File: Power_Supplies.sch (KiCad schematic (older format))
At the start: 38 parts, among them J1 Conn_HDR_2x10_latching, Q3 2N7002BK, Q4 2N7002BK, Q5 2N7002BK, Q6 2N7002BK, Q7 2N7002BK, Q8 2N7002BK, Q9 2N7002BK, U4 BD50FC0WEFJ-E2, U5 LDL212D33R, U6 LDL212D33R, U7 TLV7042DGKR

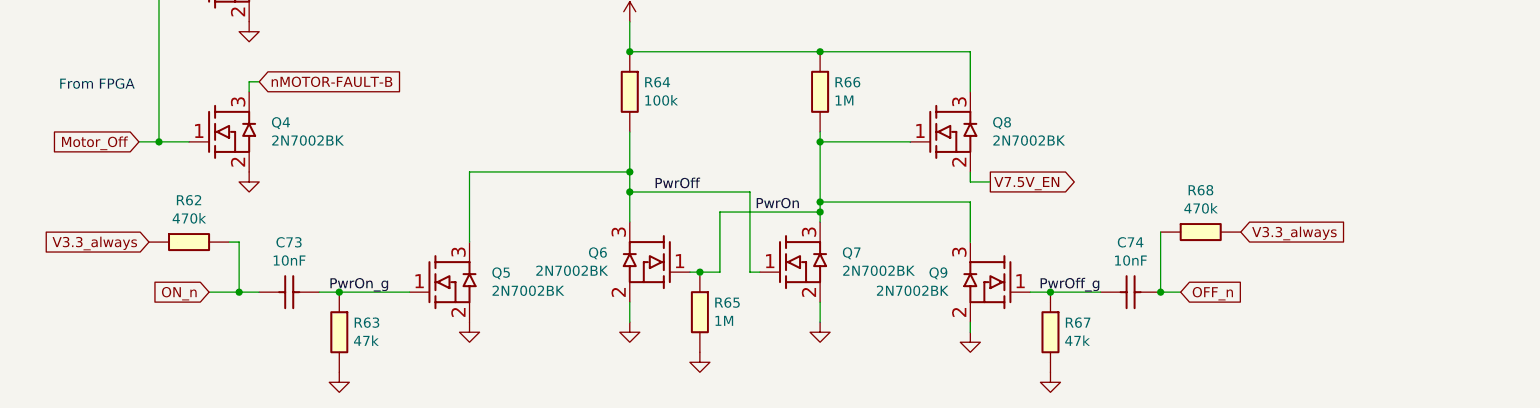
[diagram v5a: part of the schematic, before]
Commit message: Corrected power ON/OFF control circuit signal labels
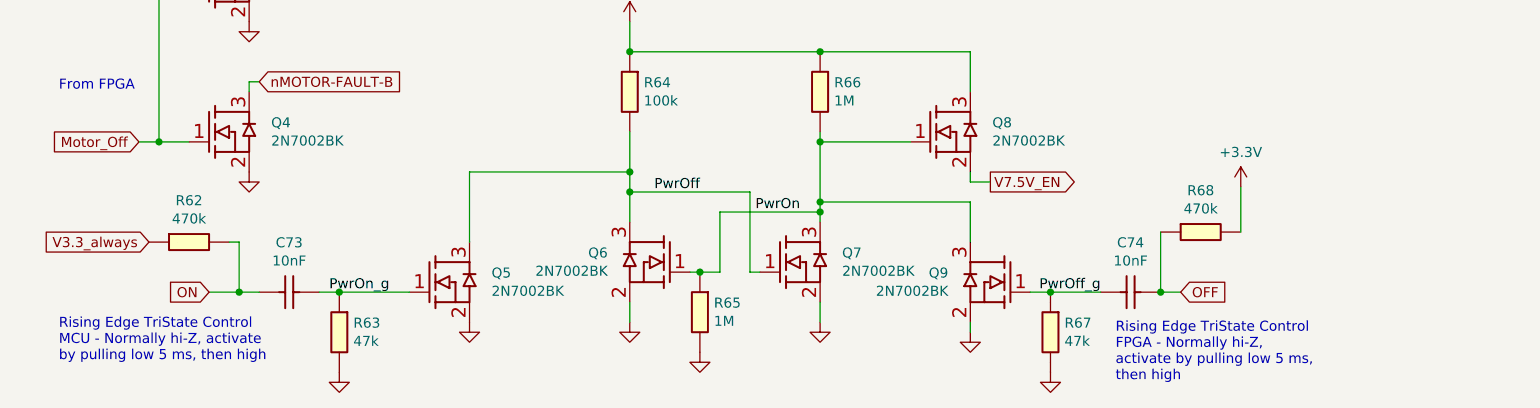
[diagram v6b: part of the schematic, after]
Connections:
- net +3V3: now also R68.2
- net V3.3_always: no longer R68.2
- net OFF_n renamed OFF
- net ON_n renamed ON
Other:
- note added: "Rising Edge TriState Control\nFPGA - Normally hi-Z,\nactivate by pulling low 5 ms,\nthen high"
- note added: "Rising Edge TriState Control\nMCU - Normally hi-Z, activate \nby pulling low 5 ms, then high"
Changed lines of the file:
@@
 	1450 7300 1550 7300
 Text GLabel 1300 7300 0    50   Input ~ 0
-ON_n
+ON
 Wire Wire Line
 	1300 7300 1450 7300
@@
 $EndComp
 Text GLabel 6150 7300 2    50   Input ~ 0
-OFF_n
+OFF
 Wire Wire Line
 	6050 7300 6150 7300
+Connection ~ 6050 7300
+Text Label 2200 7300 2    50   ~ 0
+PwrOn_g
+Text Label 3750 6800 2    50   ~ 0
+PwrOff
+Text Label 4250 6900 2    50   ~ 0
+PwrOn
+Text Label 5750 7300 2    50   ~ 0
+PwrOff_g
+$Comp
+L OpenVent:1M_0603_Chip_Resistor,_1%,_0.1W R66
+U 1 1 60119693
+P 4450 6200
+F 0 "R66" V 4504 6170 50  0000 L CNN
+F 1 "1M_0603_Chip_Resistor,_1%,_0.1W" H 4450 6200 50  0001 C CNN
+F 2 "" H 4450 6200 50  0001 C CNN
+F 3 "" H 4450 6200 50  0001 C CNN
+F 4 "1M" V 4595 6170 50  0000 L CNN "Val"
+F 5 "1%" H 4450 6200 50  0001 C CNN "Tolerance"
+F 6 "0.1W" H 4450 6200 50  0001 C CNN "Watt"
+	1    4450 6200
+	0    1    1    0
+$EndComp
+Connection ~ 4350 6550
+Wire Wire Line
+	4350 6550 4350 6850
+Connection ~ 4350 6100
+Wire Wire Line
+	4350 6100 3400 6100
+Wire Wire Line
+	4350 6500 4350 6550
+Wire Wire Line
+	3400 6700 3400 6500
+Connection ~ 3400 6700
+Wire Wire Line
+	5100 6100 5100 6300
+$Comp
+L OpenVent:1M_0603_Chip_Resistor,_1%,_0.1W R65
+U 1 1 6013F297
+P 3850 7300
+F 0 "R65" V 3904 7270 50  0000 L CNN
+F 1 "1M_0603_Chip_Resistor,_1%,_0.1W" H 3850 7300 50  0001 C CNN
+F 2 "" H 3850 7300 50  0001 C CNN
+F 3 "" H 3850 7300 50  0001 C CNN
+F 4 "1M" V 3995 7270 50  0000 L CNN "Val"
+F 5 "1%" H 3850 7300 50  0001 C CNN "Tolerance"
+F 6 "0.1W" H 3850 7300 50  0001 C CNN "Watt"
+	1    3850 7300
+	0    1    1    0
+$EndComp
+Connection ~ 3750 7200
+Wire Wire Line
+	3750 7200 3850 7200
+$Comp
+L OpenVent:47k_0603_Chip_Resistor,_1%,_0.1W R63
+U 1 1 60168217
+P 2050 7400
+F 0 "R63" V 2104 7370 50  0000 L CNN
+F 1 "47k_0603_Chip_Resistor,_1%,_0.1W" H 2050 7400 50  0001 C CNN
+F 2 "" H 2050 7400 50  0001 C CNN
+F 3 "" H 2050 7400 50  0001 C CNN
+F 4 "47k" V 2195 7370 50  0000 L CNN "Val"
+F 5 "1%" H 2050 7400 50  0001 C CNN "Tolerance"
+F 6 "0.1W" H 2050 7400 50  0001 C CNN "Watt"
+	1    2050 7400
+	0    1    1    0
+$EndComp
+$Comp
+L OpenVent:47k_0603_Chip_Resistor,_1%,_0.1W R67
+U 1 1 60168F63
+P 5600 7400
+F 0 "R67" V 5654 7370 50  0000 L CNN
+F 1 "47k_0603_Chip_Resistor,_1%,_0.1W" H 5600 7400 50  0001 C CNN
+F 2 "" H 5600 7400 50  0001 C CNN
+F 3 "" H 5600 7400 50  0001 C CNN
+F 4 "47k" V 5745 7370 50  0000 L CNN "Val"
+F 5 "1%" H 5600 7400 50  0001 C CNN "Tolerance"
+F 6 "0.1W" H 5600 7400 50  0001 C CNN "Watt"
+	1    5600 7400
+	0    1    1    0
+$EndComp
+Connection ~ 1950 7300
+Wire Wire Line
+	1950 7300 2300 7300
+Connection ~ 5500 7300
+Wire Wire Line
+	5500 7300 5750 7300
+$Comp
+L OpenVent:V_MAIN #PWR0112
+U 1 1 60198400
+P 3400 5950
+F 0 "#PWR0112" H 3400 5800 50  0001 C CNN
+F 1 "V_MAIN" H 3400 6123 50  0000 C CNN
+F 2 "" H 3400 5950 50  0001 C CNN
+F 3 "" H 3400 5950 50  0001 C CNN
+	1    3400 5950
+	1    0    0    -1
+$EndComp
+Wire Wire Line
+	3400 6100 3400 5950
+Wire Wire Line
+	1500 6300 1500 6250
+Wire Wire Line
+	1500 6250 1550 6250
+Wire Wire Line
+	1500 5550 1500 5500
+Wire Wire Line
+	1500 5500 1550 5500
+Wire Wire Line
+	5200 6750 5100 6750
+Wire Wire Line
+	5100 6750 5100 6700
+$Comp
+L OpenVent:+3.3V #PWR?
+U 1 1 6007611B
+P 6450 6775
+F 0 "#PWR?" H 6450 6625 50  0001 C CNN
+F 1 "+3.3V" H 6450 6948 50  0000 C CNN
+F 2 "" H 6450 6775 50  0001 C CNN
+F 3 "" H 6450 6775 50  0001 C CNN
+	1    6450 6775
+	1    0    0    -1
+$EndComp
 $Comp
 L OpenVent:470k_0603_Chip_Resistor,_1%,_0.1W R68
@@
 $EndComp
 Wire Wire Line
-	6050 7300 6050 7000
-Text GLabel 6450 7000 2    50   Input ~ 0
-V3.3_always
-Connection ~ 6050 7300
-Text Label 2200 7300 2    50   ~ 0
-PwrOn_g
-Text Label 3750 6800 2    50   ~ 0
-PwrOff
-Text Label 4250 6900 2    50   ~ 0
-PwrOn
-Text Label 5750 7300 2    50   ~ 0
-PwrOff_g
-$Comp
-L OpenVent:1M_0603_Chip_Resistor,_1%,_0.1W R66
-U 1 1 60119693
-P 4450 6200
-F 0 "R66" V 4504 6170 50  0000 L CNN
-F 1 "1M_0603_Chip_Resistor,_1%,_0.1W" H 4450 6200 50  0001 C CNN
-F 2 "" H 4450 6200 50  0001 C CNN
-F 3 "" H 4450 6200 50  0001 C CNN
-F 4 "1M" V 4595 6170 50  0000 L CNN "Val"
-F 5 "1%" H 4450 6200 50  0001 C CNN "Tolerance"
-F 6 "0.1W" H 4450 6200 50  0001 C CNN "Watt"
-	1    4450 6200
-	0    1    1    0
-$EndComp
-Connection ~ 4350 6550
-Wire Wire Line
-	4350 6550 4350 6850
-Connection ~ 4350 6100
-Wire Wire Line
-	4350 6100 3400 6100
-Wire Wire Line
-	4350 6500 4350 6550
-Wire Wire Line
-	3400 6700 3400 6500
-Connection ~ 3400 6700
-Wire Wire Line
-	5100 6100 5100 6300
-$Comp
-L OpenVent:1M_0603_Chip_Resistor,_1%,_0.1W R65
-U 1 1 6013F297
-P 3850 7300
-F 0 "R65" V 3904 7270 50  0000 L CNN
-F 1 "1M_0603_Chip_Resistor,_1%,_0.1W" H 3850 7300 50  0001 C CNN
-F 2 "" H 3850 7300 50  0001 C CNN
-F 3 "" H 3850 7300 50  0001 C CNN
-F 4 "1M" V 3995 7270 50  0000 L CNN "Val"
-F 5 "1%" H 3850 7300 50  0001 C CNN "Tolerance"
-F 6 "0.1W" H 3850 7300 50  0001 C CNN "Watt"
-	1    3850 7300
-	0    1    1    0
-$EndComp
-Connection ~ 3750 7200
-Wire Wire Line
-	3750 7200 3850 7200
-$Comp
-L OpenVent:47k_0603_Chip_Resistor,_1%,_0.1W R63
-U 1 1 60168217
-P 2050 7400
-F 0 "R63" V 2104 7370 50  0000 L CNN
-F 1 "47k_0603_Chip_Resistor,_1%,_0.1W" H 2050 7400 50  0001 C CNN
-F 2 "" H 2050 7400 50  0001 C CNN
-F 3 "" H 2050 7400 50  0001 C CNN
-F 4 "47k" V 2195 7370 50  0000 L CNN "Val"
-F 5 "1%" H 2050 7400 50  0001 C CNN "Tolerance"
-F 6 "0.1W" H 2050 7400 50  0001 C CNN "Watt"
-	1    2050 7400
-	0    1    1    0
-$EndComp
-$Comp
-L OpenVent:47k_0603_Chip_Resistor,_1%,_0.1W R67
-U 1 1 60168F63
-P 5600 7400
-F 0 "R67" V 5654 7370 50  0000 L CNN
-F 1 "47k_0603_Chip_Resistor,_1%,_0.1W" H 5600 7400 50  0001 C CNN
-F 2 "" H 5600 7400 50  0001 C CNN
-F 3 "" H 5600 7400 50  0001 C CNN
-F 4 "47k" V 5745 7370 50  0000 L CNN "Val"
-F 5 "1%" H 5600 7400 50  0001 C CNN "Tolerance"
-F 6 "0.1W" H 5600 7400 50  0001 C CNN "Watt"
-	1    5600 7400
-	0    1    1    0
-$EndComp
-Connection ~ 1950 7300
-Wire Wire Line
-	1950 7300 2300 7300
-Connection ~ 5500 7300
-Wire Wire Line
-	5500 7300 5750 7300
-$Comp
-L OpenVent:V_MAIN #PWR0112
-U 1 1 60198400
-P 3400 5950
-F 0 "#PWR0112" H 3400 5800 50  0001 C CNN
-F 1 "V_MAIN" H 3400 6123 50  0000 C CNN
-F 2 "" H 3400 5950 50  0001 C CNN
-F 3 "" H 3400 5950 50  0001 C CNN
-	1    3400 5950
-	1    0    0    -1
-$EndComp
-Wire Wire Line
-	3400 6100 3400 5950
-Wire Wire Line
-	1500 6300 1500 6250
-Wire Wire Line
-	1500 6250 1550 6250
-Wire Wire Line
-	1500 5550 1500 5500
-Wire Wire Line
-	1500 5500 1550 5500
-Wire Wire Line
-	5200 6750 5100 6750
-Wire Wire Line
-	5100 6750 5100 6700
+	6050 7000 6050 7300
+Wire Wire Line
+	6450 7000 6450 6775
+Text Notes 5825 7750 0    50   ~ 0
+Rising Edge TriState Control\nFPGA - Normally hi-Z,\nactivate by pulling low 5 ms,\nthen high
+Text Notes 550  7650 0    50   ~ 0
+Rising Edge TriState Control\nMCU - Normally hi-Z, activate \nby pulling low 5 ms, then high
 $EndSCHEMATC

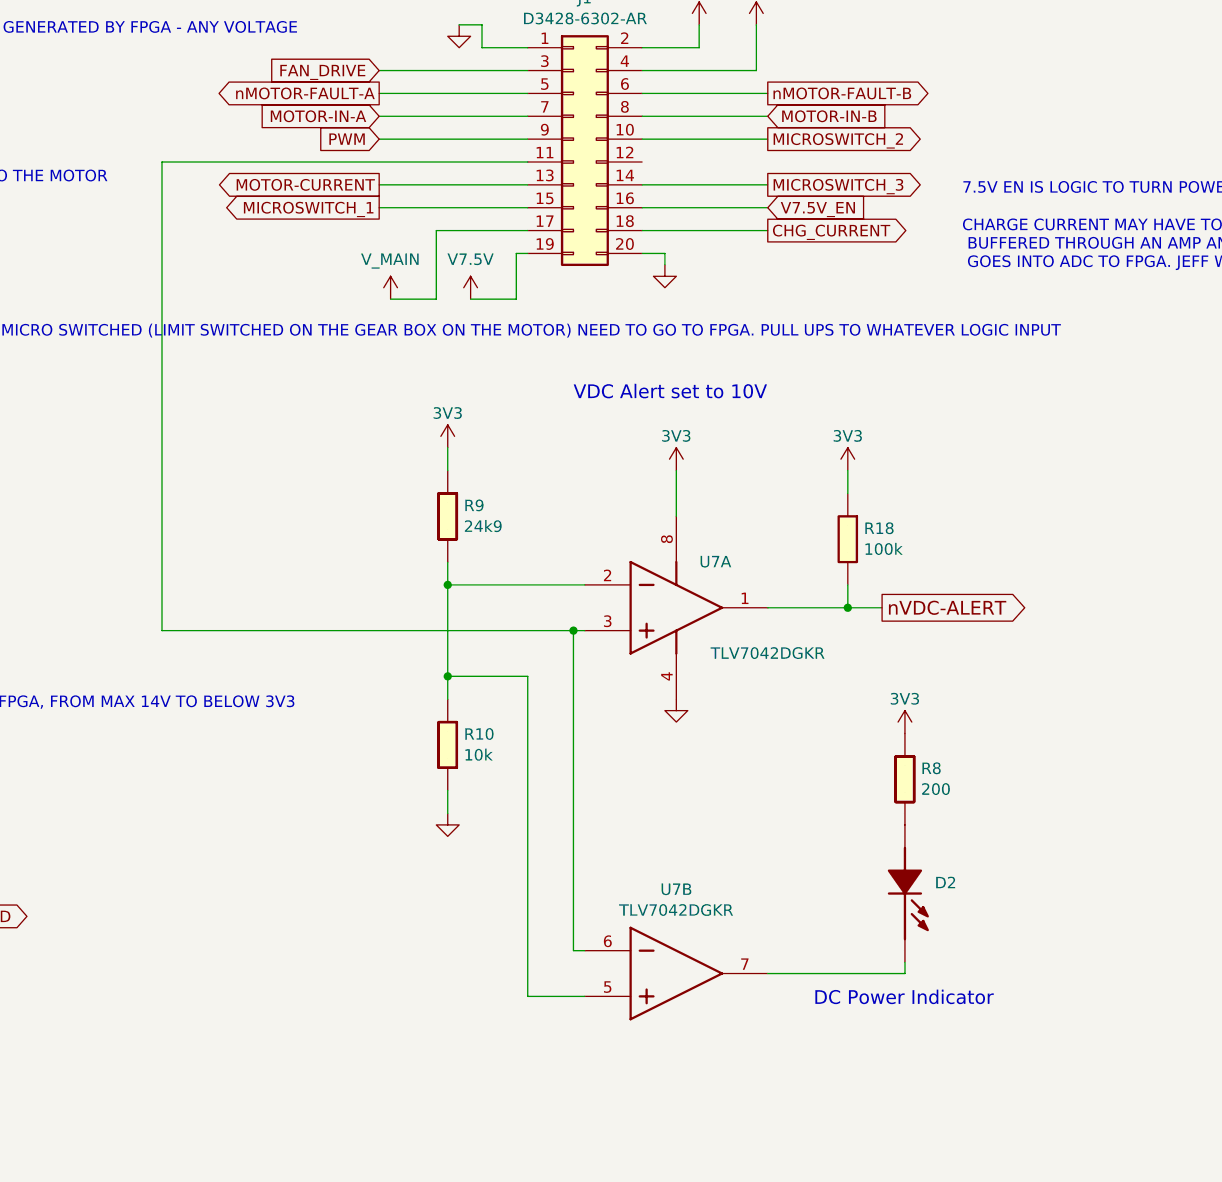
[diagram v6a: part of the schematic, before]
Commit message: Alerts and ISNS signals removed
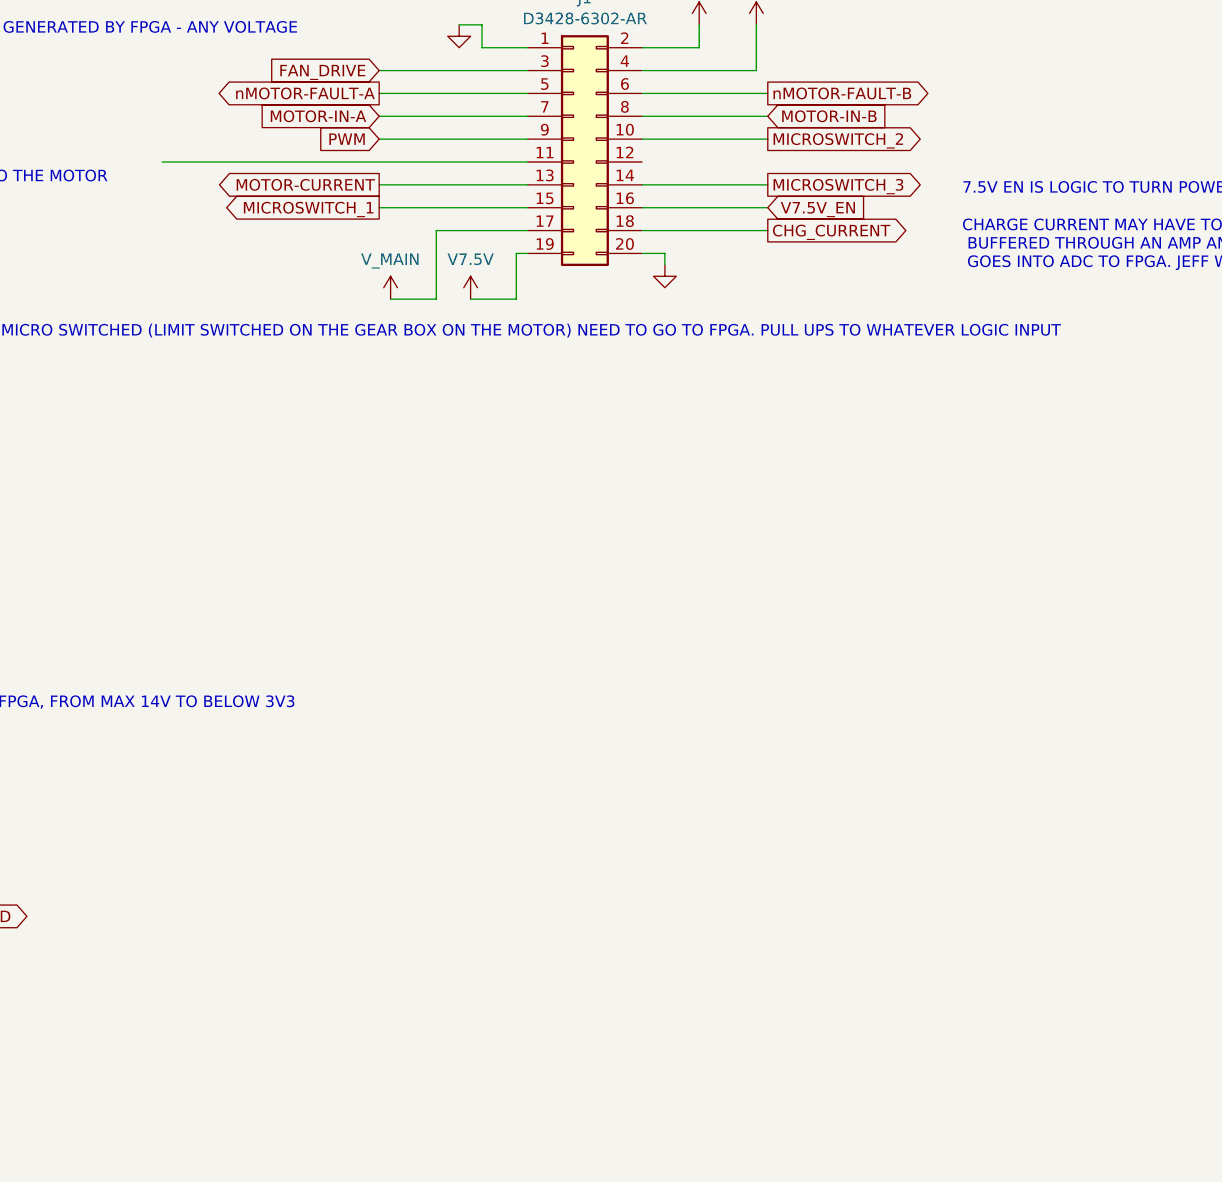
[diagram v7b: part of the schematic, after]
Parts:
- removed D2: LED_GREEN_0603_SMD, LED_SMD:LED_0603_1608Metric, symbol OpenVent:LED_GREEN_0603_SMD
- removed R10: 10k_0603_Chip_Resistor,_1%,_0.1W, Resistor_SMD:R_0603_1608Metric, symbol OpenVent:10k_0603_Chip_Resistor,_1%,_0.1W
- removed R18: 100K_0603_Chip_Resistor,_1%,_0.1W, Resistor_SMD:R_0603_1608Metric, symbol OpenVent:100K_0603_Chip_Resistor,_1%,_0.1W
- removed R8: R_0603_200_0.1W_1%, Resistor_SMD:R_0603_1608Metric, symbol OpenVent:R_0603_200_0.1W_1%
- removed R9: R_0603_24k9_0.1W_1%, symbol OpenVent:R_0603_24k9_0.1W_1%
- removed U7: TLV7042DGKR, F_ICs:Texas_S-PDSO-G8, symbol OpenVent:TLV7042DGKR
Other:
- note removed: "DC Power Indicator"
- note removed: "VDC Alert set to 10V"
